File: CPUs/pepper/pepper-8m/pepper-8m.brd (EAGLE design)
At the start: 48.2 x 25.4 mm, 22 parts

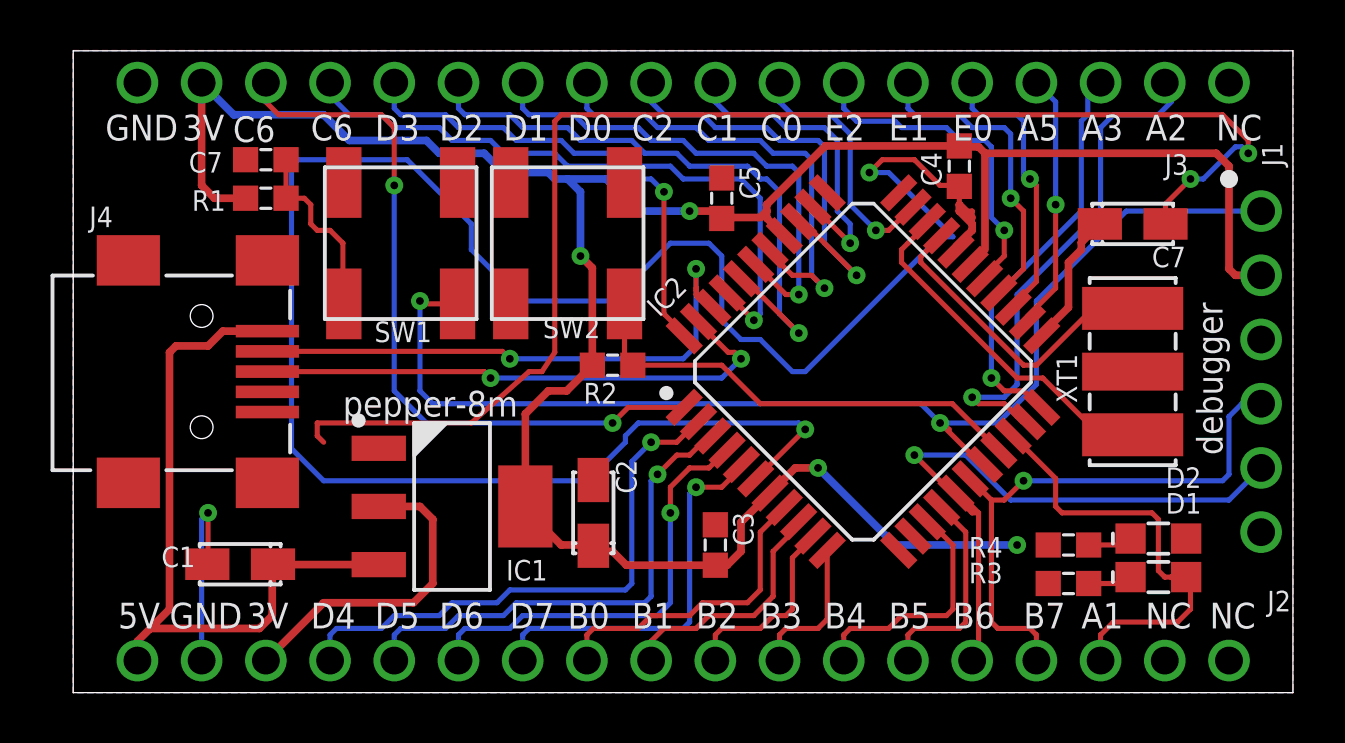
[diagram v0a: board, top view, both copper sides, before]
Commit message: this is version 0.2
the board is only 0.1" shorter and the silscreeen was corected in oreder
o add part numbers
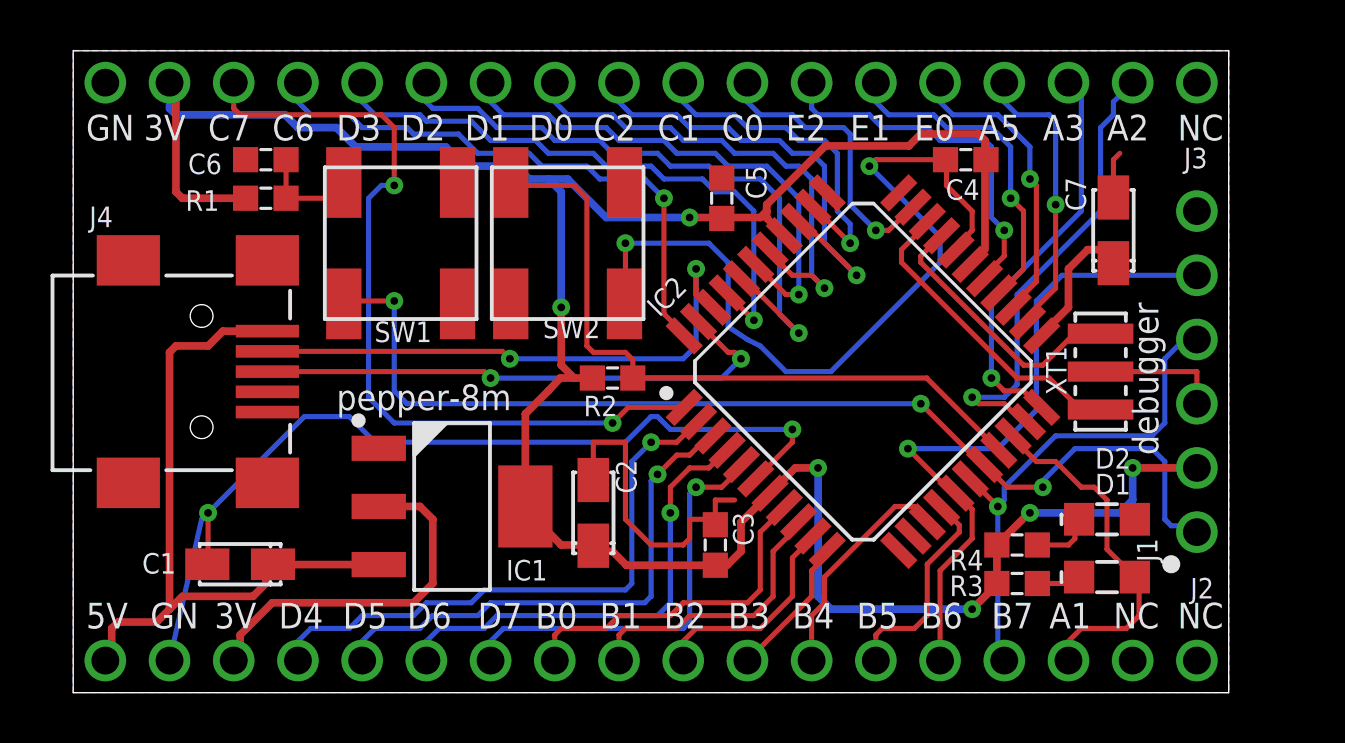
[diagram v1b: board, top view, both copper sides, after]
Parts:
- XT1: device abracon-resonators:CERAMIC740X340-3N -> abracon-resonators:CERAMIC460X200-3N
- moved J1 13.0 mm to (44.5, 6.35), turned to 90 degrees
- moved D2 2.17 mm to (40.9, 6.86)
- moved D1 2.03 mm to (40.9, 4.57)
- moved R3 2.03 mm to (37.3, 4.32)
- moved R4 2.03 mm to (37.3, 5.84)
- moved J2 1.27 mm to (44.5, 1.27)
- moved J3 1.27 mm to (44.5, 24.1)
- moved XT1 1.27 mm to (40.6, 12.7)
- moved C7 0.80 mm to (41.1, 18.3), turned to 270 degrees
- moved R2 0.51 mm to (21.3, 12.4)
- moved C4 0.36 mm to (35.3, 21.1), turned to 0 degrees
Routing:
- net GND: track 148.3 -> 88.2 mm, vias 5 -> 4
- net BTN: track 20.0 -> 28.5 mm
- net RESET: track 54.6 -> 46.6 mm, vias 2 -> 3
- net +3V3: track 113.9 -> 121.4 mm, vias 4 -> 6
- net LED: track 17.9 -> 13.9 mm
- net C7: track 29.1 -> 32.4 mm
- net XTAL: track 15.3 -> 12.3 mm
- net PGD: track 22.6 -> 20.1 mm
- net A2: track 20.2 -> 18.4 mm
- net EXTAL: track 12.4 -> 10.7 mm
- net PGC: track 25.5 -> 27.0 mm
- net B1: track 9.69 -> 11.1 mm
- net B0: track 12.3 -> 13.5 mm
- net A5: track 10.0 -> 11.3 mm
- net E2: track 13.2 -> 14.5 mm
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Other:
- board size 48.2 x 25.4 mm -> 45.7 x 25.4 mm
- board text added: "GN"
- board text removed: "GND"
